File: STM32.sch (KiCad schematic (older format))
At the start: 1 part

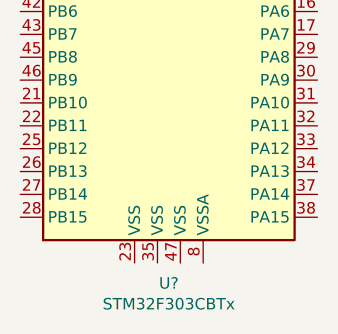
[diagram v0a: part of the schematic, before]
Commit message: Added all stepper circuits. Adding SPI bus to top level sheet. Opened up layout to check connectivity. Errors with footprint libs
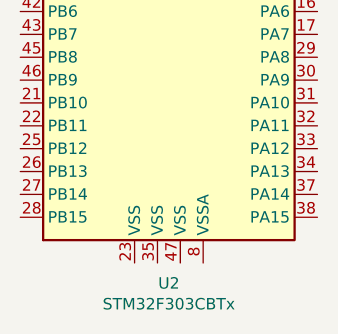
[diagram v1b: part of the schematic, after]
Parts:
- gave numbers to parts that had none: 1
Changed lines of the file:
@@
 EESchema Schematic File Version 4
-LIBS:bountifulHarvest-cache
-EELAYER 26 0
+EELAYER 30 0
 EELAYER END
 $Descr A4 11693 8268
 encoding utf-8
-Sheet 3 6
+Sheet 3 7
 Title ""
 Date ""
@@
 $EndDescr
 $Comp
-L MCU_ST_STM32F3:STM32F303CBTx U?
+L MCU_ST_STM32F3:STM32F303CBTx U2
 U 1 1 5EE72350
 P 5750 3750
-F 0 "U?" H 5700 2161 50  0000 C CNN
+F 0 "U2" H 5700 2161 50  0000 C CNN
 F 1 "STM32F303CBTx" H 5700 2070 50  0000 C CNN
 F 2 "Package_QFP:LQFP-48_7x7mm_P0.5mm" H 5150 2350 50  0001 R CNN

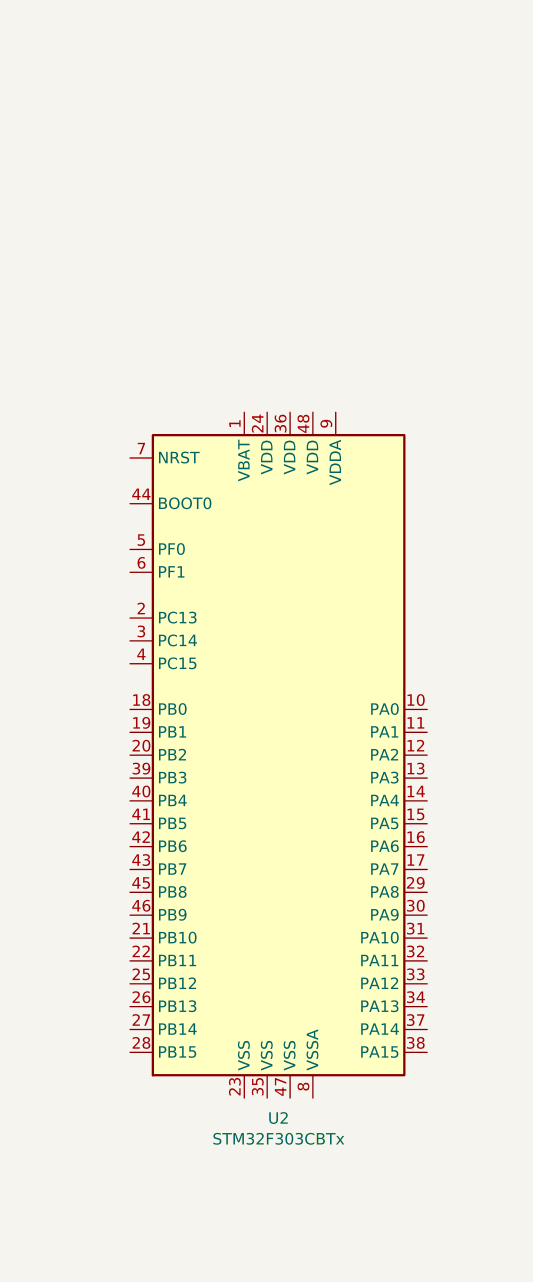
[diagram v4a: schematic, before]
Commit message: updated ATMEGA and regulators
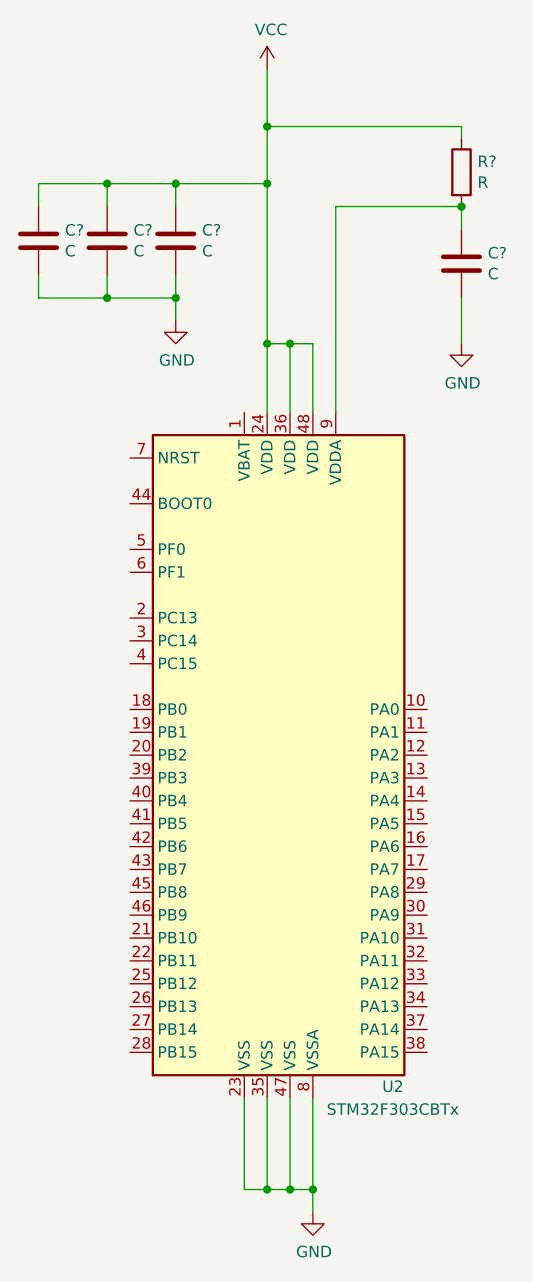
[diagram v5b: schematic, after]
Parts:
- added C? (x4): C, symbol Device:C
- added R?: R, symbol Device:R
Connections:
- net GND: now reaches U2.23 (VSS)
- net GND: now also U2.35 (VSS), U2.47 (VSS), U2.8 (VSSA), C?.2, C?.2, C?.2, C?.2
- net VCC: now reaches U2.24 (VDD)
- net VCC: now also U2.36 (VDD), U2.48 (VDD), C?.1, C?.1, C?.1, R?.1
- net at U2.9 (VDDA): now also C?.1, R?.2
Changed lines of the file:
@@
 U 1 1 5EE72350
 P 5750 3750
-F 0 "U2" H 5700 2161 50  0000 C CNN
-F 1 "STM32F303CBTx" H 5700 2070 50  0000 C CNN
+F 0 "U2" H 6200 2300 50  0000 C CNN
+F 1 "STM32F303CBTx" H 6200 2200 50  0000 C CNN
 F 2 "Package_QFP:LQFP-48_7x7mm_P0.5mm" H 5150 2350 50  0001 R CNN
 F 3 "http://www.st.com/st-web-ui/static/active/en/resource/technical/document/datasheet/DM00058181.pdf" H 5750 3750 50  0001 C CNN
@@
 	1    0    0    -1
 $EndComp
+$Comp
+L power:VCC #PWR?
+U 1 1 622767A2
+P 5650 750
+AR Path="/5EE66603/622767A2" Ref="#PWR?"  Part="1"
+AR Path="/5EE7212D/622767A2" Ref="#PWR?"  Part="1"
+F 0 "#PWR?" H 5650 600 50  0001 C CNN
+F 1 "VCC" H 5667 923 50  0000 C CNN
+F 2 "" H 5650 750 50  0001 C CNN
+F 3 "" H 5650 750 50  0001 C CNN
+	1    5650 750
+	1    0    0    -1
+$EndComp
+Wire Wire Line
+	5850 2250 5850 1950
+Wire Wire Line
+	5850 1950 5750 1950
+Wire Wire Line
+	5650 1950 5650 2250
+Wire Wire Line
+	5750 2250 5750 1950
+Connection ~ 5750 1950
+Wire Wire Line
+	5750 1950 5650 1950
+$Comp
+L Device:C C?
+U 1 1 622776A0
+P 5250 1500
+AR Path="/5EE66603/622776A0" Ref="C?"  Part="1"
+AR Path="/5EE7212D/622776A0" Ref="C?"  Part="1"
+F 0 "C?" H 5365 1546 50  0000 L CNN
+F 1 "C" H 5365 1455 50  0000 L CNN
+F 2 "" H 5288 1350 50  0001 C CNN
+F 3 "~" H 5250 1500 50  0001 C CNN
+	1    5250 1500
+	1    0    0    -1
+$EndComp
+$Comp
+L power:GND #PWR?
+U 1 1 62277BAE
+P 5250 1850
+AR Path="/5EE66603/62277BAE" Ref="#PWR?"  Part="1"
+AR Path="/5EE7212D/62277BAE" Ref="#PWR?"  Part="1"
+F 0 "#PWR?" H 5250 1600 50  0001 C CNN
+F 1 "GND" H 5255 1677 50  0000 C CNN
+F 2 "" H 5250 1850 50  0001 C CNN
+F 3 "" H 5250 1850 50  0001 C CNN
+	1    5250 1850
+	1    0    0    -1
+$EndComp
+Wire Wire Line
+	5250 1650 5250 1750
+Connection ~ 5650 1950
+Wire Wire Line
+	5250 1350 5250 1250
+Wire Wire Line
+	5250 1250 5650 1250
+Connection ~ 5650 1250
+Wire Wire Line
+	5650 1250 5650 1000
+$Comp
+L Device:C C?
+U 1 1 62279383
+P 4950 1500
+AR Path="/5EE66603/62279383" Ref="C?"  Part="1"
+AR Path="/5EE7212D/62279383" Ref="C?"  Part="1"
+F 0 "C?" H 5065 1546 50  0000 L CNN
+F 1 "C" H 5065 1455 50  0000 L CNN
+F 2 "" H 4988 1350 50  0001 C CNN
+F 3 "~" H 4950 1500 50  0001 C CNN
+	1    4950 1500
+	1    0    0    -1
+$EndComp
+$Comp
+L Device:C C?
+U 1 1 62279669
+P 4650 1500
+AR Path="/5EE66603/62279669" Ref="C?"  Part="1"
+AR Path="/5EE7212D/62279669" Ref="C?"  Part="1"
+F 0 "C?" H 4765 1546 50  0000 L CNN
+F 1 "C" H 4765 1455 50  0000 L CNN
+F 2 "" H 4688 1350 50  0001 C CNN
+F 3 "~" H 4650 1500 50  0001 C CNN
+	1    4650 1500
+	1    0    0    -1
+$EndComp
+Wire Wire Line
+	4650 1650 4650 1750
+Wire Wire Line
+	4650 1750 4950 1750
+Connection ~ 5250 1750
+Wire Wire Line
+	5250 1750 5250 1850
+Wire Wire Line
+	4950 1650 4950 1750
+Connection ~ 4950 1750
+Wire Wire Line
+	4950 1750 5250 1750
+Wire Wire Line
+	5250 1250 4950 1250
+Wire Wire Line
+	4650 1250 4650 1350
+Connection ~ 5250 1250
+Wire Wire Line
+	4950 1350 4950 1250
+Connection ~ 4950 1250
+Wire Wire Line
+	4950 1250 4650 1250
+$Comp
+L Device:R R?
+U 1 1 6227B935
+P 6500 1200
+F 0 "R?" H 6570 1246 50  0000 L CNN
+F 1 "R" H 6570 1155 50  0000 L CNN
+F 2 "" V 6430 1200 50  0001 C CNN
+F 3 "~" H 6500 1200 50  0001 C CNN
+	1    6500 1200
+	1    0    0    -1
+$EndComp
+Wire Wire Line
+	6500 1050 6500 1000
+$Comp
+L Device:C C?
+U 1 1 6227D077
+P 6500 1600
+AR Path="/5EE66603/6227D077" Ref="C?"  Part="1"
+AR Path="/5EE7212D/6227D077" Ref="C?"  Part="1"
+F 0 "C?" H 6615 1646 50  0000 L CNN
+F 1 "C" H 6615 1555 50  0000 L CNN
+F 2 "" H 6538 1450 50  0001 C CNN
+F 3 "~" H 6500 1600 50  0001 C CNN
+	1    6500 1600
+	1    0    0    -1
+$EndComp
+$Comp
+L power:GND #PWR?
+U 1 1 6227D07D
+P 6500 1950
+AR Path="/5EE66603/6227D07D" Ref="#PWR?"  Part="1"
+AR Path="/5EE7212D/6227D07D" Ref="#PWR?"  Part="1"
+F 0 "#PWR?" H 6500 1700 50  0001 C CNN
+F 1 "GND" H 6505 1777 50  0000 C CNN
+F 2 "" H 6500 1950 50  0001 C CNN
+F 3 "" H 6500 1950 50  0001 C CNN
+	1    6500 1950
+	1    0    0    -1
+$EndComp
+Wire Wire Line
+	6500 1750 6500 1950
+Wire Wire Line
+	5650 1250 5650 1950
+Wire Wire Line
+	5650 1000 6500 1000
+Connection ~ 5650 1000
+Wire Wire Line
+	5650 1000 5650 750
+Wire Wire Line
+	6500 1350 5950 1350
+Wire Wire Line
+	5950 1350 5950 2250
+Wire Wire Line
+	6500 1450 6500 1350
+Connection ~ 6500 1350
+$Comp
+L power:GND #PWR?
+U 1 1 622818A4
+P 5850 5750
+AR Path="/5EE66603/622818A4" Ref="#PWR?"  Part="1"
+AR Path="/5EE7212D/622818A4" Ref="#PWR?"  Part="1"
+F 0 "#PWR?" H 5850 5500 50  0001 C CNN
+F 1 "GND" H 5855 5577 50  0000 C CNN
+F 2 "" H 5850 5750 50  0001 C CNN
+F 3 "" H 5850 5750 50  0001 C CNN
+	1    5850 5750
+	1    0    0    -1
+$EndComp
+Wire Wire Line
+	5550 5250 5550 5650
+Wire Wire Line
+	5550 5650 5650 5650
+Wire Wire Line
+	5850 5650 5850 5250
+Wire Wire Line
+	5750 5250 5750 5650
+Connection ~ 5750 5650
+Wire Wire Line
+	5750 5650 5850 5650
+Wire Wire Line
+	5650 5250 5650 5650
+Connection ~ 5650 5650
+Wire Wire Line
+	5650 5650 5750 5650
+Wire Wire Line
+	5850 5750 5850 5650
+Connection ~ 5850 5650
 $EndSCHEMATC

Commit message: added differential RX
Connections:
- net labels added: X0_A_ENC, X0_B_ENC, X1_A_ENC, X1_B_ENC, Y_A_ENC, Y_B_ENC, Z_A_ENC, Z_B_ENC
- wire segments 34 -> 42
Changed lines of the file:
@@
 $Descr A4 11693 8268
 encoding utf-8
-Sheet 2 7
+Sheet 2 8
 Title ""
 Date ""
@@
 	5850 5750 5850 5650
 Connection ~ 5850 5650
+Text HLabel 1500 1350 2    79   Output ~ 0
+X0_A_ENC
+Text HLabel 1500 1650 2    79   Output ~ 0
+X0_B_ENC
+Text HLabel 1450 2450 2    79   Output ~ 0
+X1_A_ENC
+Text HLabel 1450 2750 2    79   Output ~ 0
+X1_B_ENC
+Wire Wire Line
+	1500 1350 950  1350
+Wire Wire Line
+	1500 1650 950  1650
+Wire Wire Line
+	1450 2450 950  2450
+Wire Wire Line
+	1450 2750 950  2750
+Text HLabel 1450 3200 2    79   Output ~ 0
+Y_A_ENC
+Text HLabel 1450 3500 2    79   Output ~ 0
+Y_B_ENC
+Text HLabel 1400 4300 2    79   Output ~ 0
+Z_A_ENC
+Text HLabel 1400 4600 2    79   Output ~ 0
+Z_B_ENC
+Wire Wire Line
+	1450 3200 900  3200
+Wire Wire Line
+	1450 3500 900  3500
+Wire Wire Line
+	1400 4300 900  4300
+Wire Wire Line
+	1400 4600 900  4600
 $EndSCHEMATC

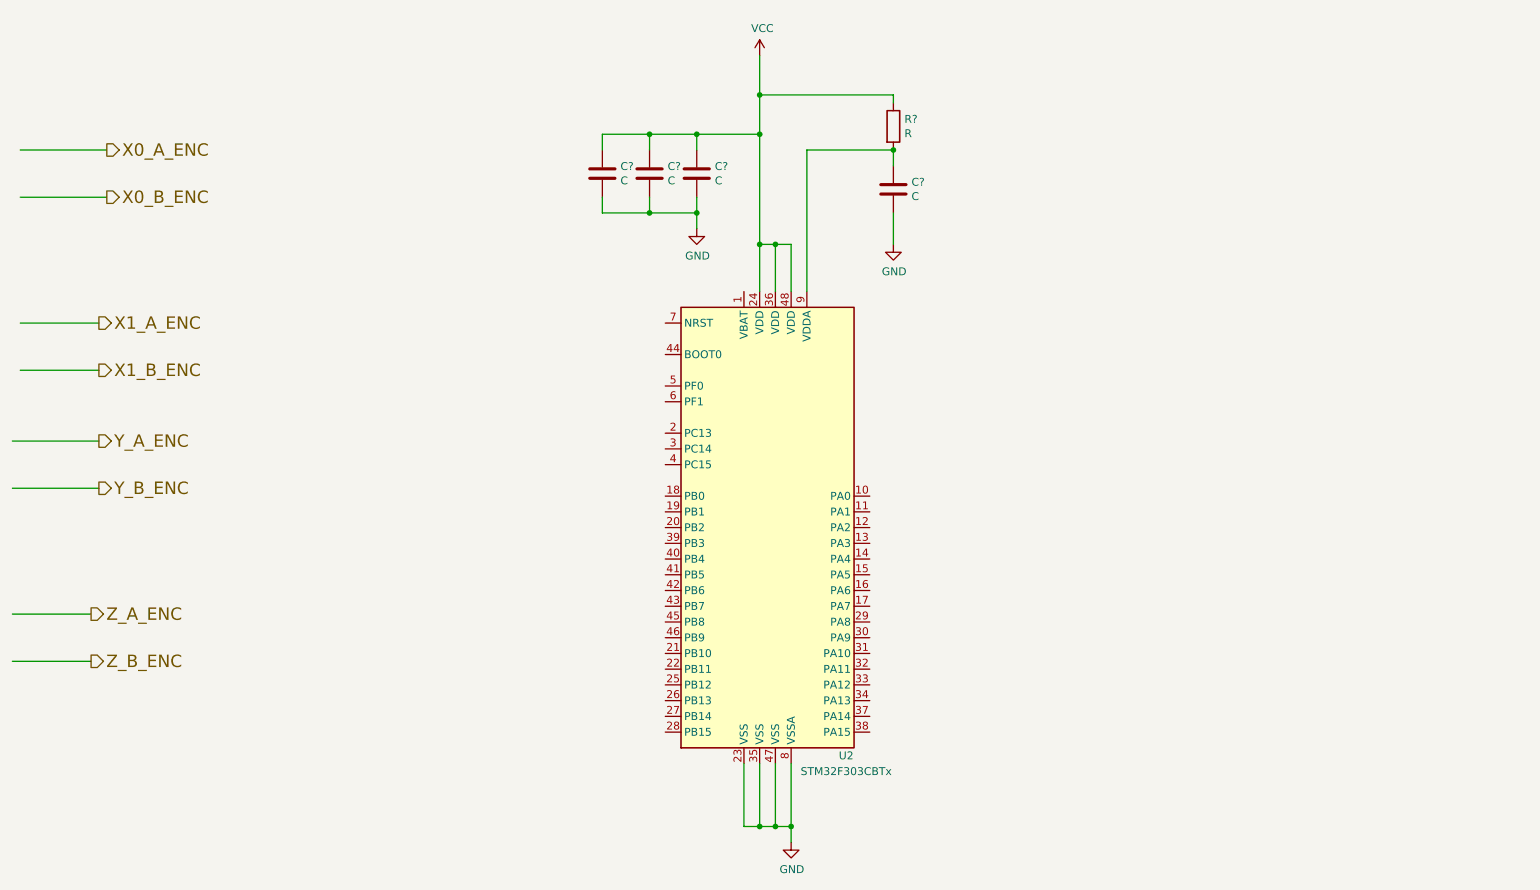
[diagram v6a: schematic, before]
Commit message: Added motor feedback to stm32. added comms/boot to stm32
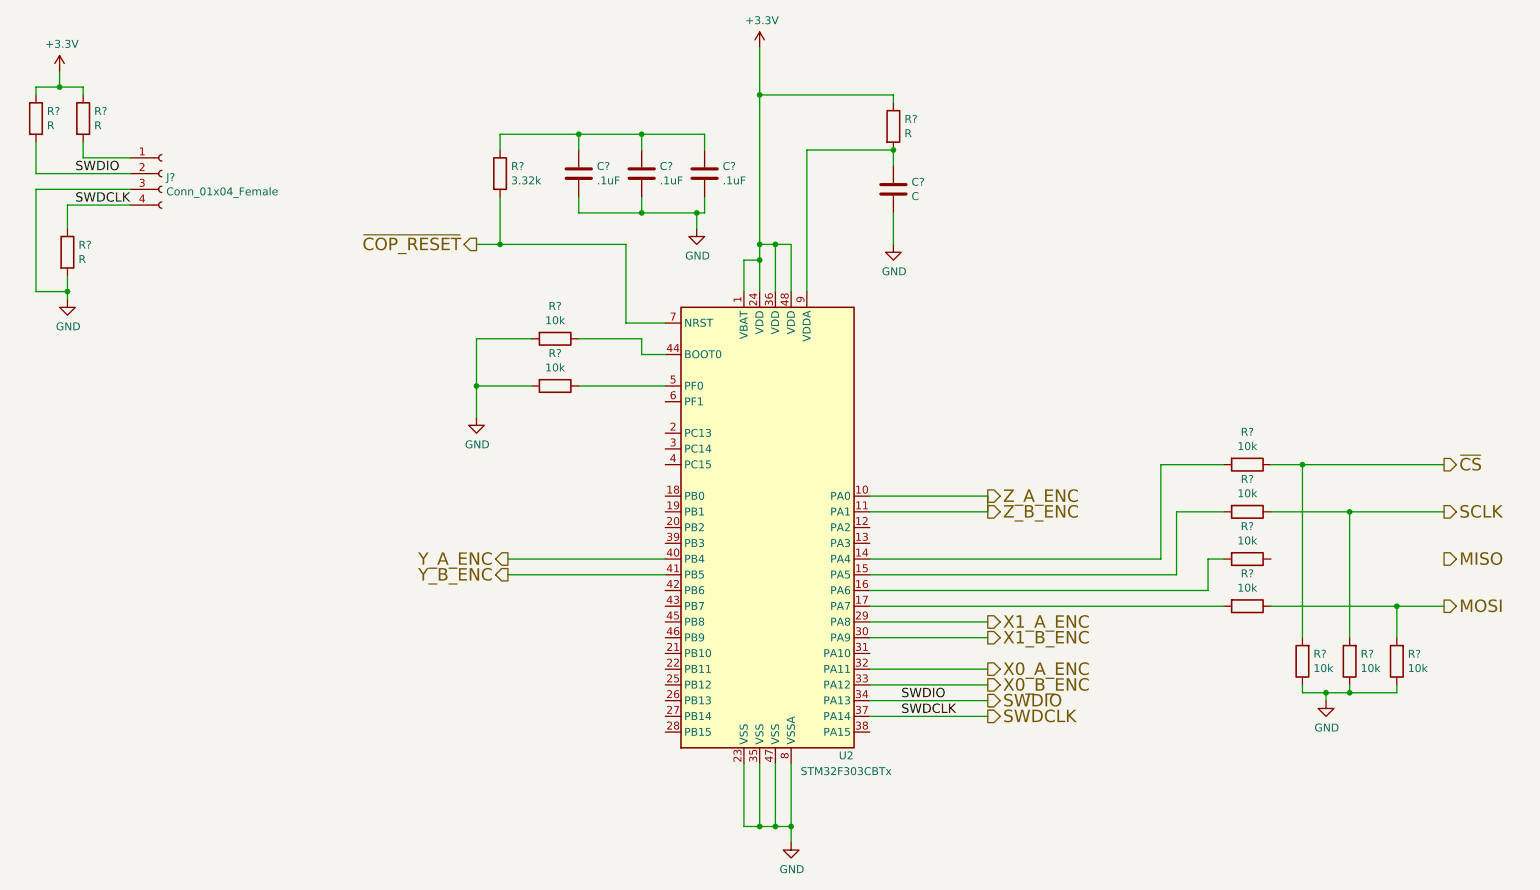
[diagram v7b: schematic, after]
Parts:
- removed C? (x2): C, symbol Device:C
- added C? (x2): .1uF, Resistor_SMD:R_0805_2012Metric_Pad1.15x1.40mm_HandSolder, symbol Device:C
- added J?: Conn_01x04_Female, symbol Connector:Conn_01x04_Female
- added R?: 3.32k, Resistor_SMD:R_0805_2012Metric_Pad1.15x1.40mm_HandSolder, symbol Device:R
- added R? (x9): 10k, Resistor_SMD:R_0805_2012Metric_Pad1.15x1.40mm_HandSolder, symbol Device:R
- added R? (x3): R, symbol Device:R
- C?: value C -> .1uF; footprint (none) -> Resistor_SMD:R_0805_2012Metric_Pad1.15x1.40mm_HandSolder
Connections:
- net labels added: +3.3V, MISO, MOSI, SCLK, SWDCLK, SWDIO, ~COP_RESET, ~CS
- net labels removed: VCC
- wire segments 42 -> 104
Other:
- moved on the sheet: C?
